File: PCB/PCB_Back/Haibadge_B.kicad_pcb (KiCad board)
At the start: 2 copper layers, 79.8 x 79.8 mm, 77 parts, among them J1 Sensor connector, J2 USB_C_Receptacle_USB2.0, J3 Lipo connector, Q1 UMH3N, Q3 Q_PMOS_GSD, SW1 SW_Push_Dual, SW2 SW_PWR, U1 ESP-12E, U2 CH340C, U3 MCP73831-2-OT, U4 MCP1700x-330xxTT, U6 BME680

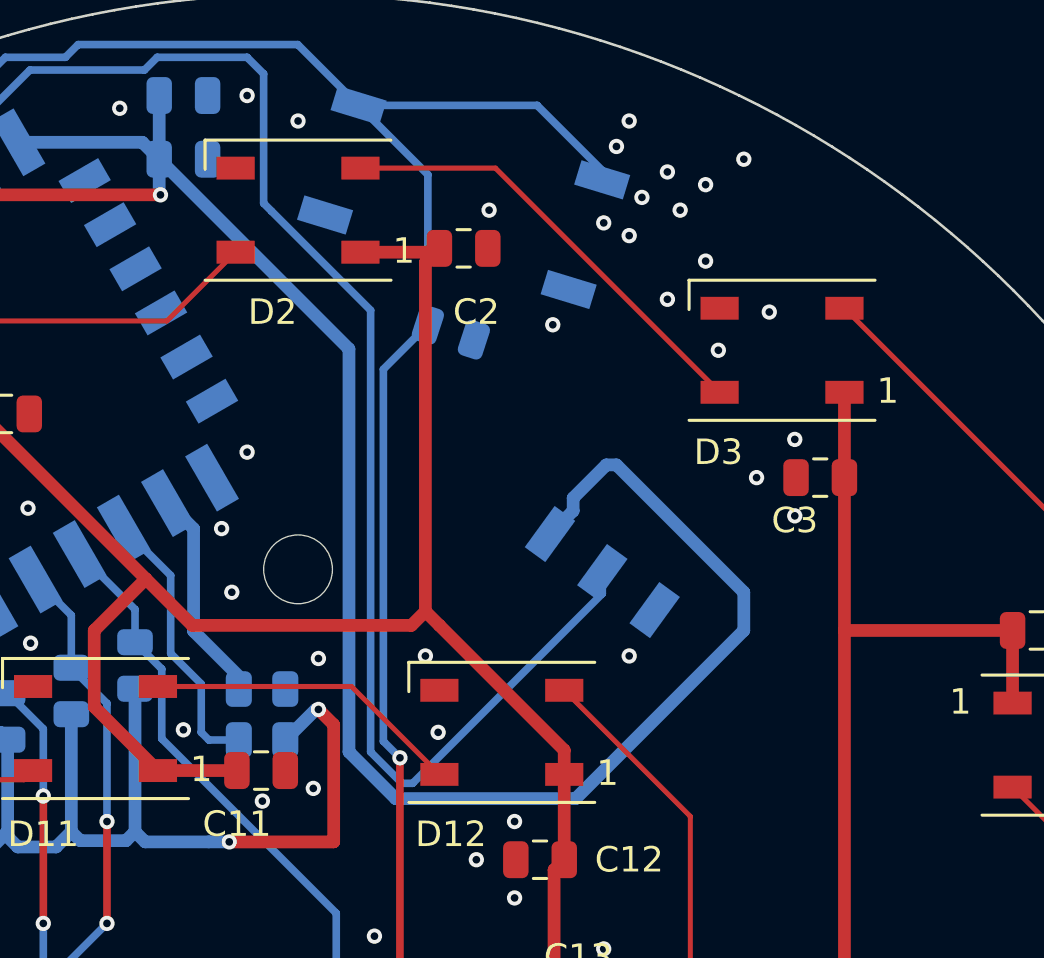
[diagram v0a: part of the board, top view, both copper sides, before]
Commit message: Back corrections, Front Edge Cut bigger.
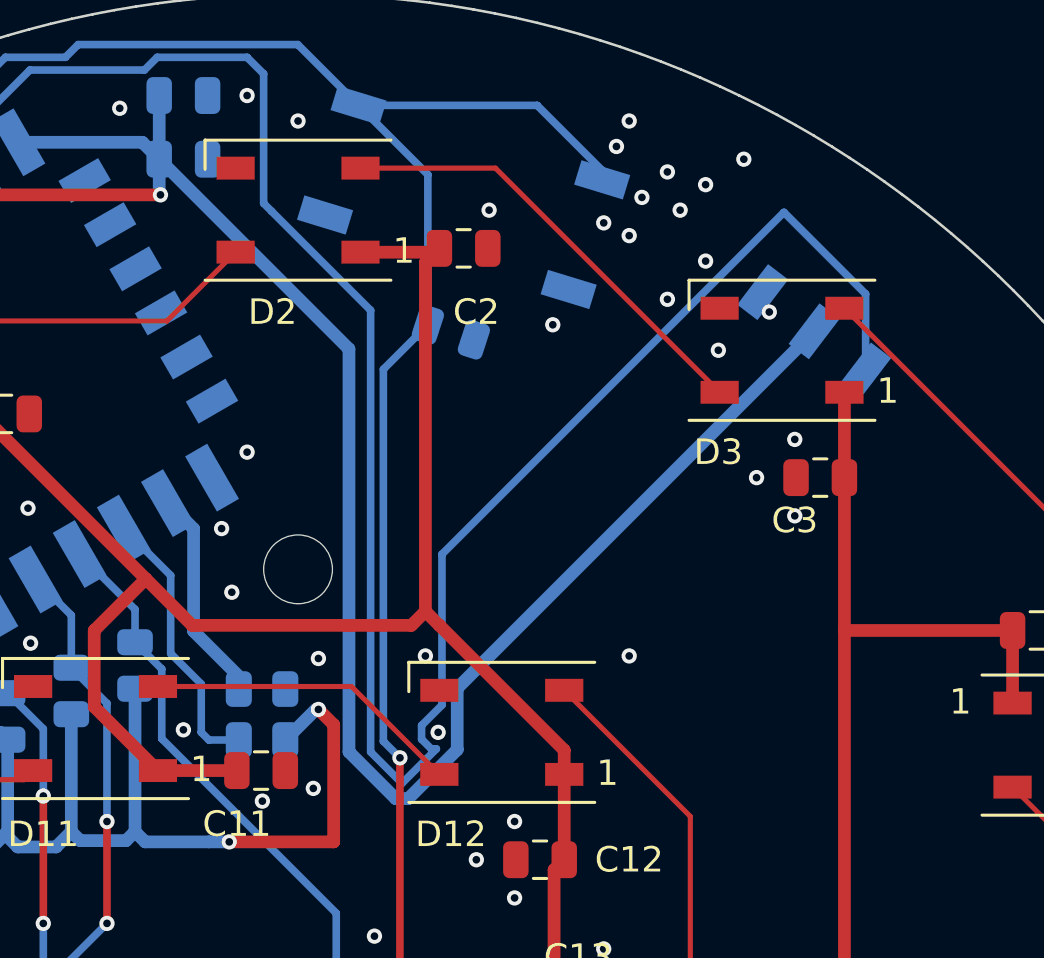
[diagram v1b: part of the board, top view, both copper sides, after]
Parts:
- moved J1 12.6 mm to (160.3, 113.3), turned to -37.3 degrees
- moved ? 0.82 mm to (185.6, 100.5)
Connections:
- J1 pad 1: +3V3 -> GND
- J1 pad 2: Sensor -> +3V3
- J1 pad 3: GND -> Sensor
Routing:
- net Sensor: track 56.3 -> 81.3 mm
- net +3V3: track 263.4 -> 259.8 mm
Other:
- board text added: "Data"

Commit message: Production ready commit
Production Version 3 commit
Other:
- board text added: "Blahaj Pentagramm Badge v3.0 (2025) Waldo und vielleicht Peter und wahrscheinlich auch Mona"
- board text removed: "Blahaj Pentagramm Badge v2.0 (2024) Waldo und vielleicht Peter"
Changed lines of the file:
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@@
 		)
 	)
-	(gr_text "Blahaj Pentagramm Badge\nv2.0 (2024)\nWaldo\nund\nvielleicht Peter"
-		(at 166 157.5 270)
+	(gr_text "Blahaj Pentagramm Badge\nv3.0 (2025)\nWaldo\nund\nvielleicht Peter\nund wahrscheinlich auch Mona"
+		(at 165.243 156.763 270)
 		(layer "B.SilkS")
 		(effects
